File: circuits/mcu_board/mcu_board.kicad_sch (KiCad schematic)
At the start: 80 parts, among them J1 USB_B_Micro, J2 Conn_01x15_Socket, J3 Conn_01x04_Pin, SW1 SW_Push, SW10 SW_Push, SW11 SW_Push, SW12 SW_Push, SW13 SW_Push, SW14 SW_Push, SW3 SW_Push, SW4 SW_Push, SW5 SW_Push, SW6 SW_Push, SW7 SW_Push, SW8 SW_Push, SW9 SW_Push, U1 STM32F302CCTx, U3 74HC165, U4 74HC165, U5 AMS1117-3.3, Y1 8MHz

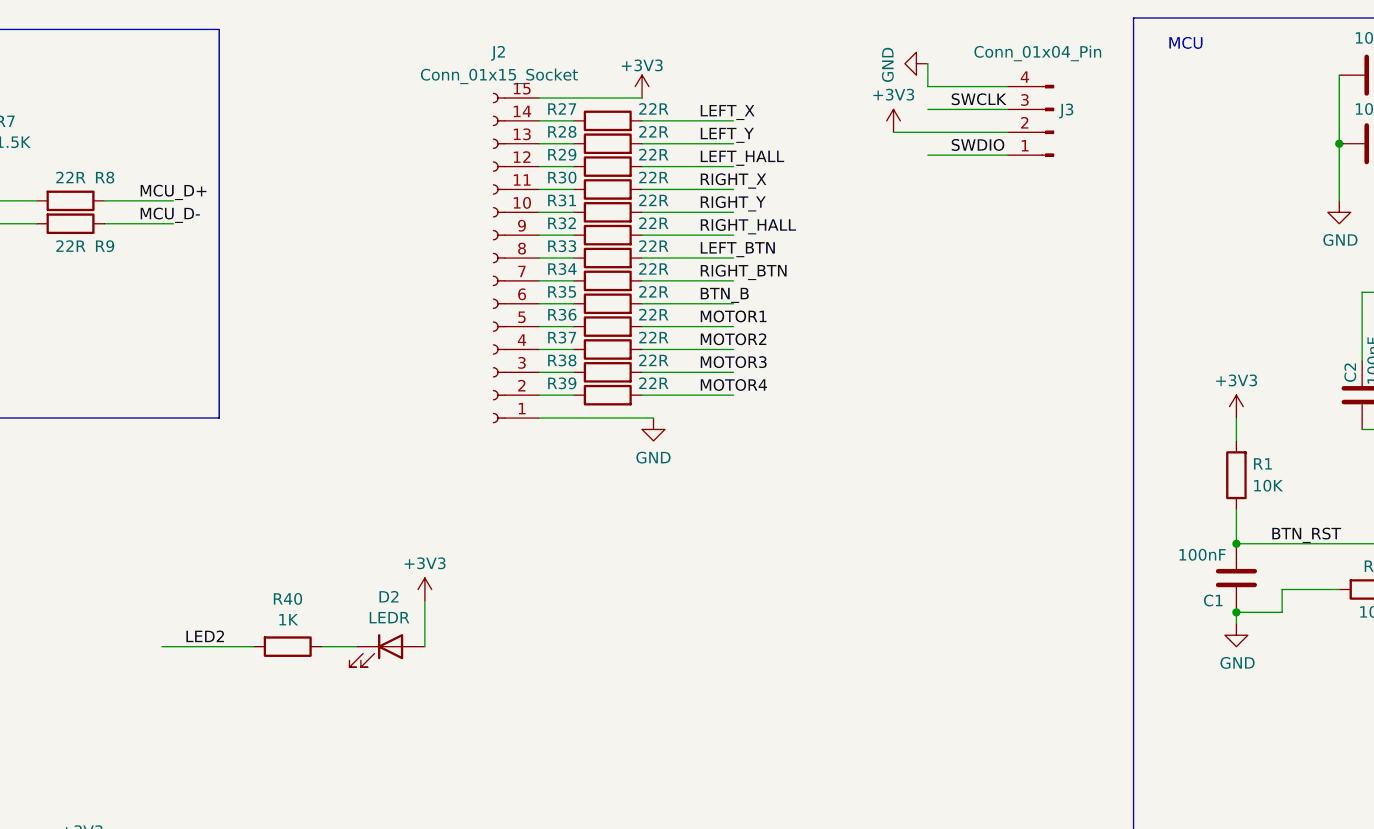
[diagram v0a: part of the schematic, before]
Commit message: pwm和led初步测试ok
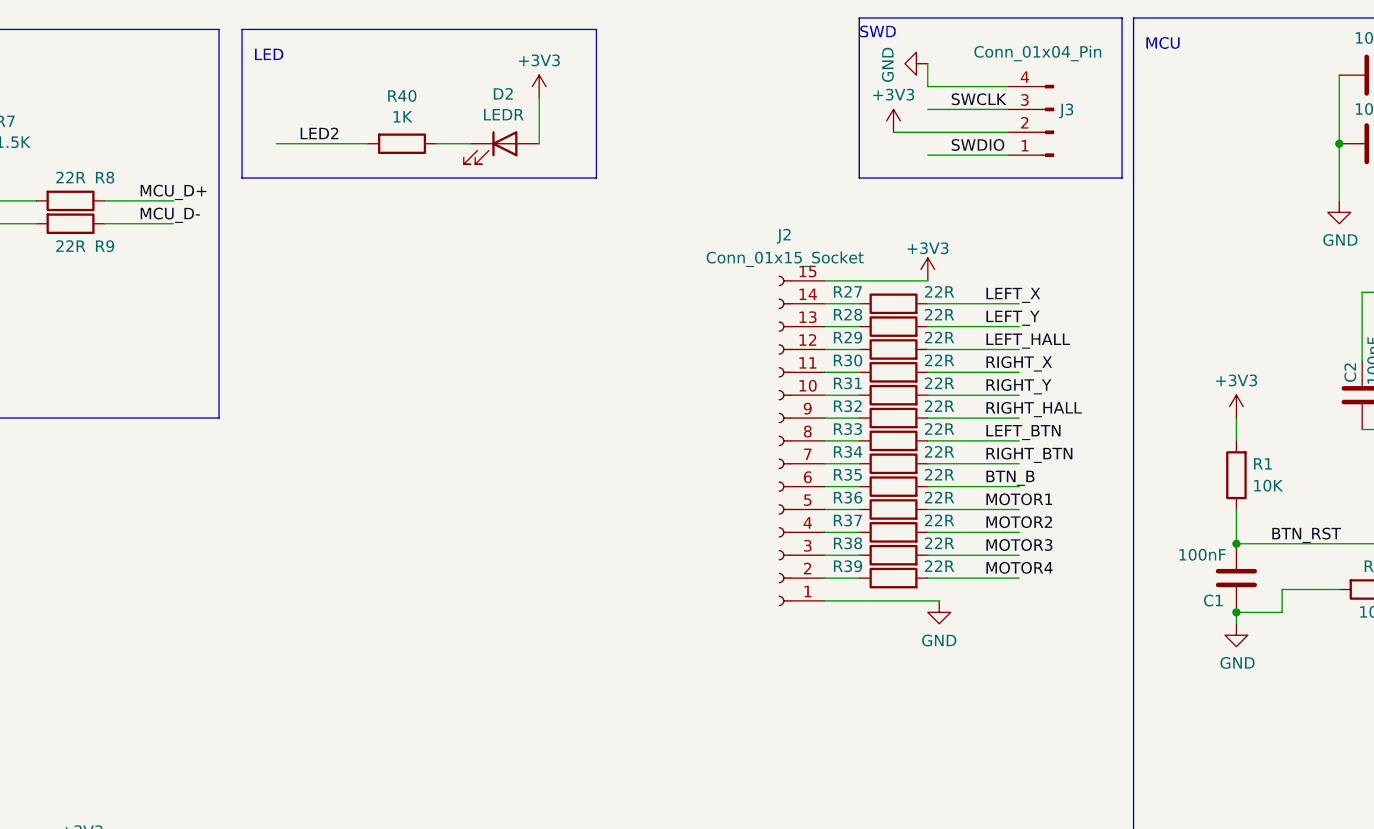
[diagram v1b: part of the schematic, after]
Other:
- note added: "LED"
- note added: "SWD"
- moved on the sheet: D2, J2, R27, R28, R29, R30, R31, R32, R33, R34, R35, R36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

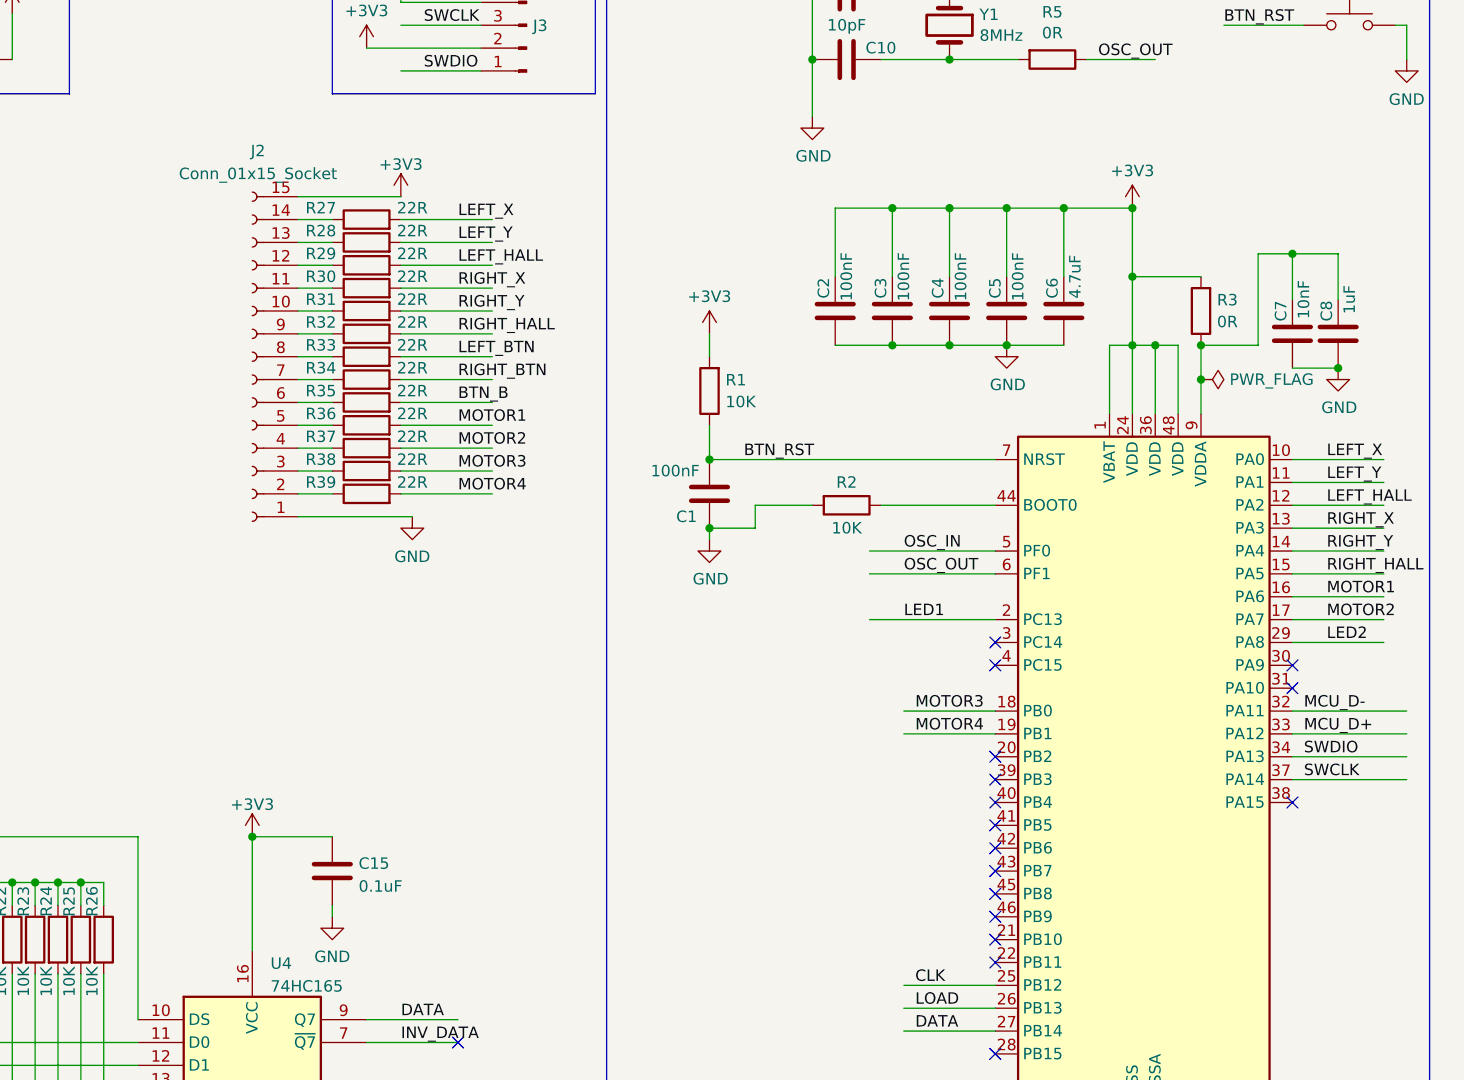
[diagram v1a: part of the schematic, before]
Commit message: layout  摇杆板优化马达驱动,增加覆铜过孔         MCU板改动
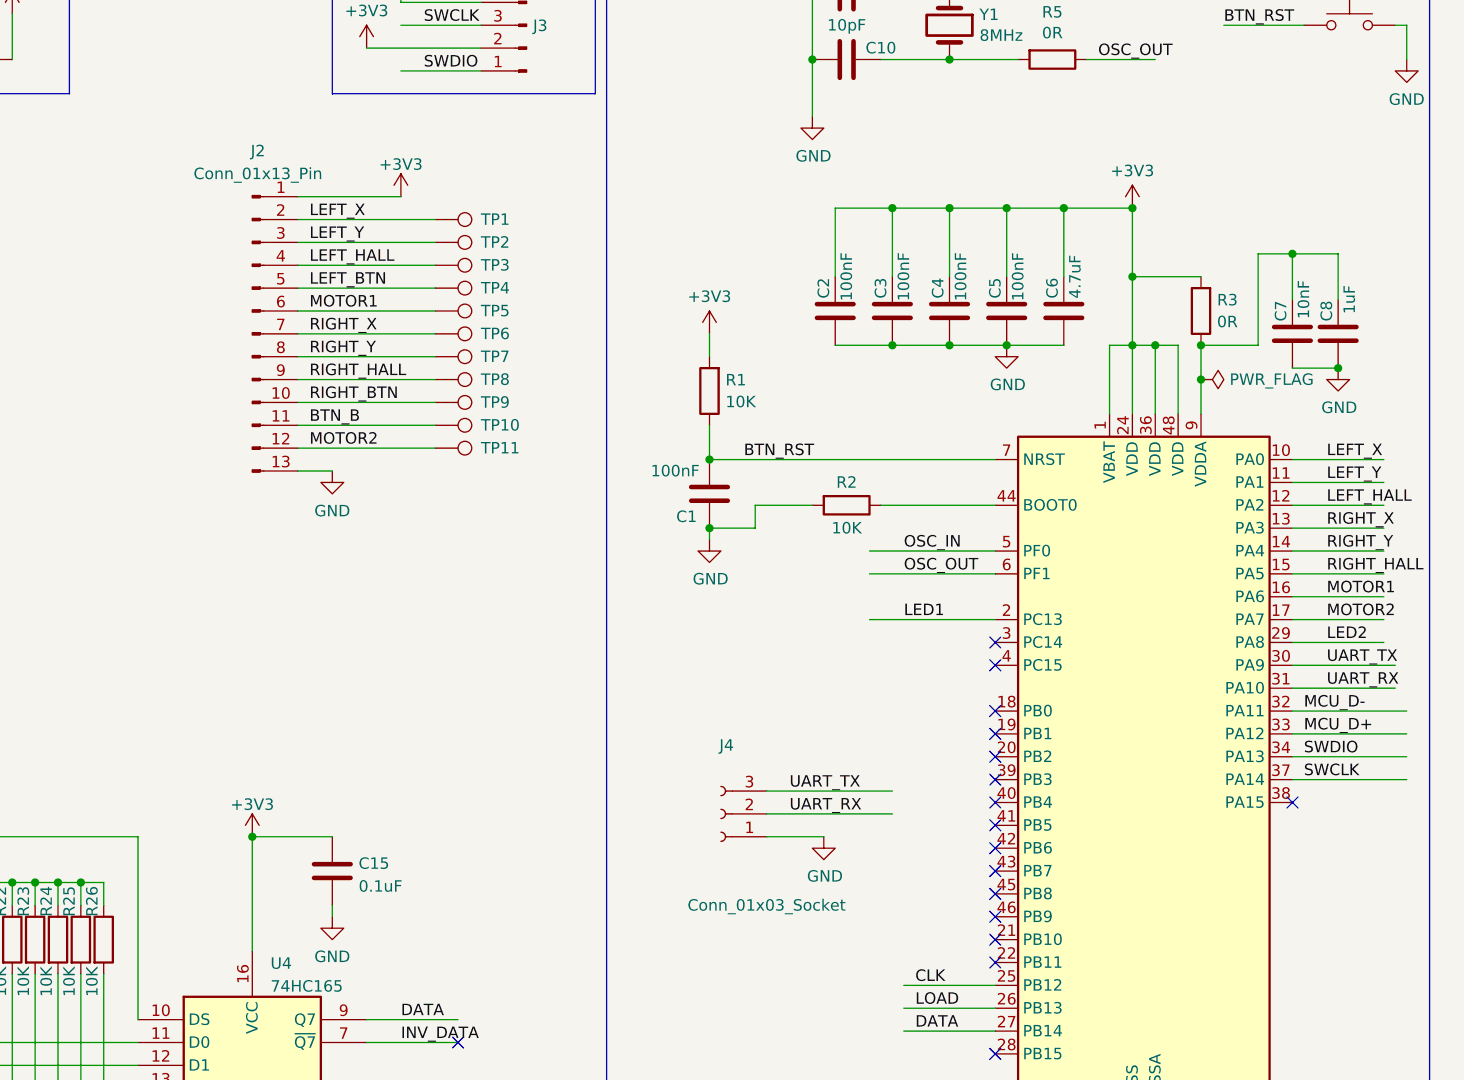
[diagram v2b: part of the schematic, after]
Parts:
- removed J2: Conn_01x15_Socket, symbol Connector:Conn_01x15_Socket
- removed R27, R28, R29, R30, R31, R32, R33, R34, R35, R36, R37, R38, R39: 22R, symbol Device:R
- added J2: Conn_01x13_Pin, Connector_FFC-FPC:Molex_200528-0130_1x13-1MP_P1.00mm_Horizontal, symbol Connector:Conn_01x13_Pin
- added J4: Conn_01x03_Socket, Connector_PinSocket_2.54mm:PinSocket_1x03_P2.54mm_Vertical, symbol Connector:Conn_01x03_Socket
- added TP1, TP10, TP11, TP2, TP3, TP4, TP5, TP6, TP7, TP8, TP9: TestPoint, TestPoint:TestPoint_Pad_1.5x1.5mm, symbol Connector:TestPoint
- C12, C16: footprint (none) -> Capacitor_SMD:C_1206_3216Metric_Pad1.33x1.80mm_HandSolder
- C14, C15: footprint Resistor_SMD:R_0805_2012Metric_Pad1.20x1.40mm_HandSolder -> Capacitor_SMD:C_0805_2012Metric_Pad1.18x1.45mm_HandSolder
- D3: footprint (none) -> Diode_SMD:D_2010_5025Metric_Pad1.52x2.65mm_HandSolder
- SW1, SW10, SW11, SW12, SW13, SW14, SW3, SW4, SW5, SW6, SW7, SW8, SW9: footprint Button_Switch_SMD:SW_Push_1P1T_NO_6x6mm_H9.5mm -> (none)
- SW_Push1: footprint Button_Switch_THT:SW_PUSH_6mm_H4.3mm -> Button_Switch_SMD:SW_Push_1P1T_NO_6x6mm_H9.5mm
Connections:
- net +3V3: now also J2.1 (Pin_1)
- net BTN_B: now also J2.11 (Pin_11), TP10.1
- net GND: now also J2.13 (Pin_13), J4.1 (Pin_1)
- net LEFT_BTN: now also J2.5 (Pin_5), TP4.1
- net LEFT_HALL: now also J2.4 (Pin_4), TP3.1
- net LEFT_X: now also J2.2 (Pin_2), TP1.1
- net LEFT_Y: now also J2.3 (Pin_3), TP2.1
- net MOTOR1: now also J2.6 (Pin_6), TP5.1
- net MOTOR2: now also J2.12 (Pin_12), TP11.1
- net RIGHT_BTN: now also J2.10 (Pin_10), TP9.1
- net RIGHT_HALL: now also J2.9 (Pin_9), TP8.1
- net RIGHT_X: now also J2.7 (Pin_7), TP6.1
- net RIGHT_Y: now also J2.8 (Pin_8), TP7.1
- net UART_TX: now reaches U1.30 (PA9)
- net UART_TX: now also J4.3 (Pin_3)
- net UART_RX: now reaches U1.31 (PA10)
- net UART_RX: now also J4.2 (Pin_2)
- net MOTOR3: no longer names the net of U1.18 (PB0)
- net MOTOR4: no longer names the net of U1.19 (PB1)

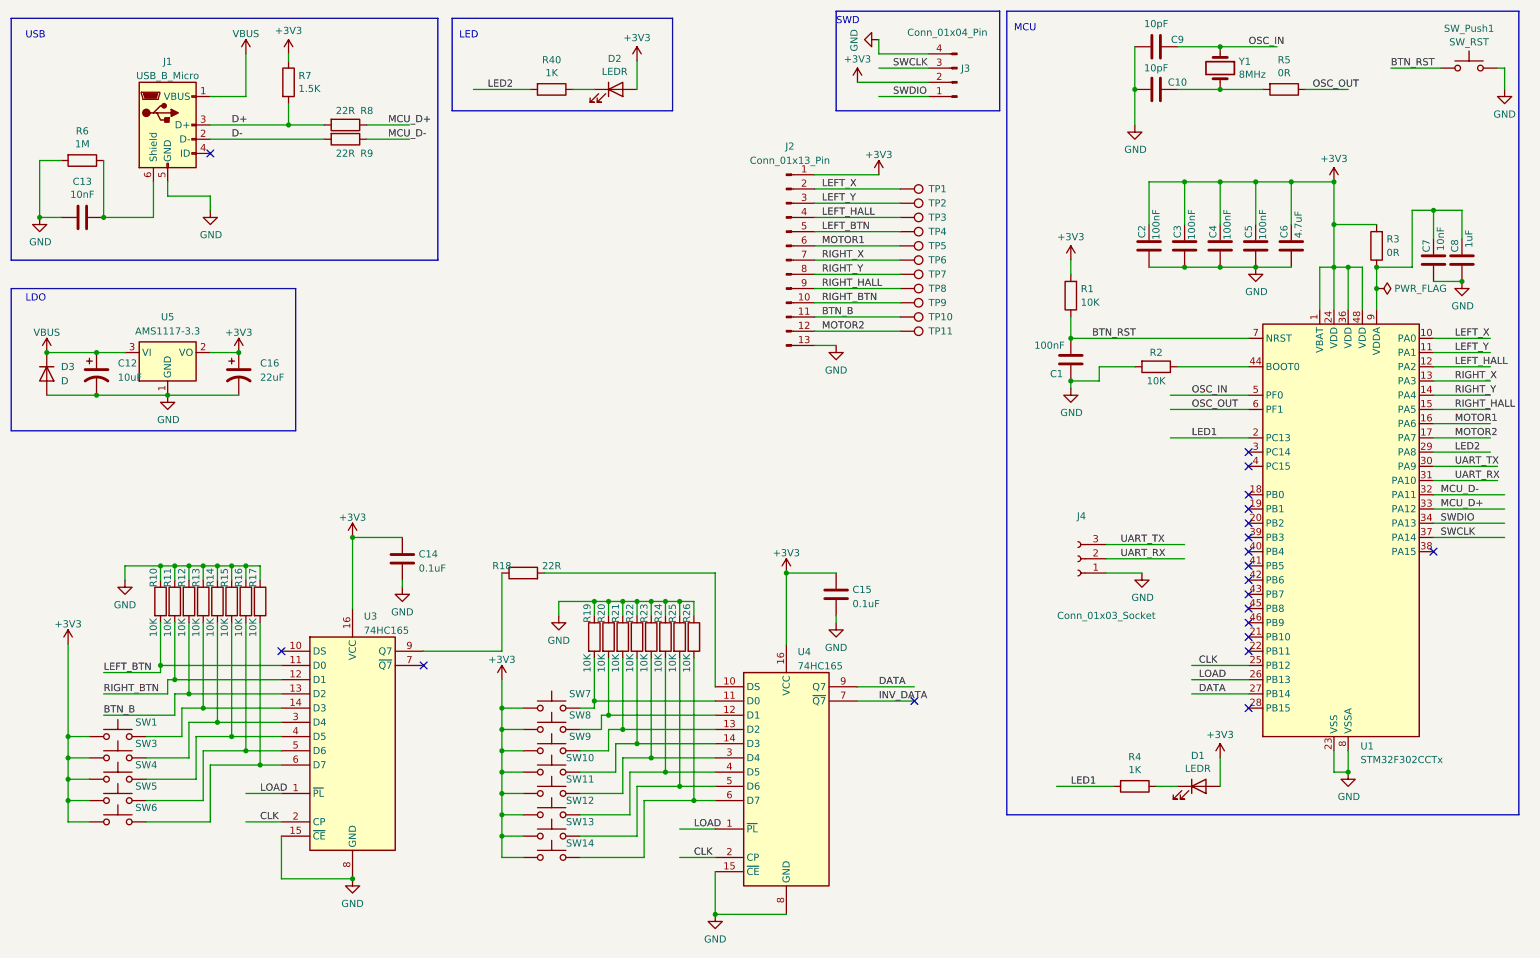
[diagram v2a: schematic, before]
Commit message: mcu板 螺丝孔位置需验证
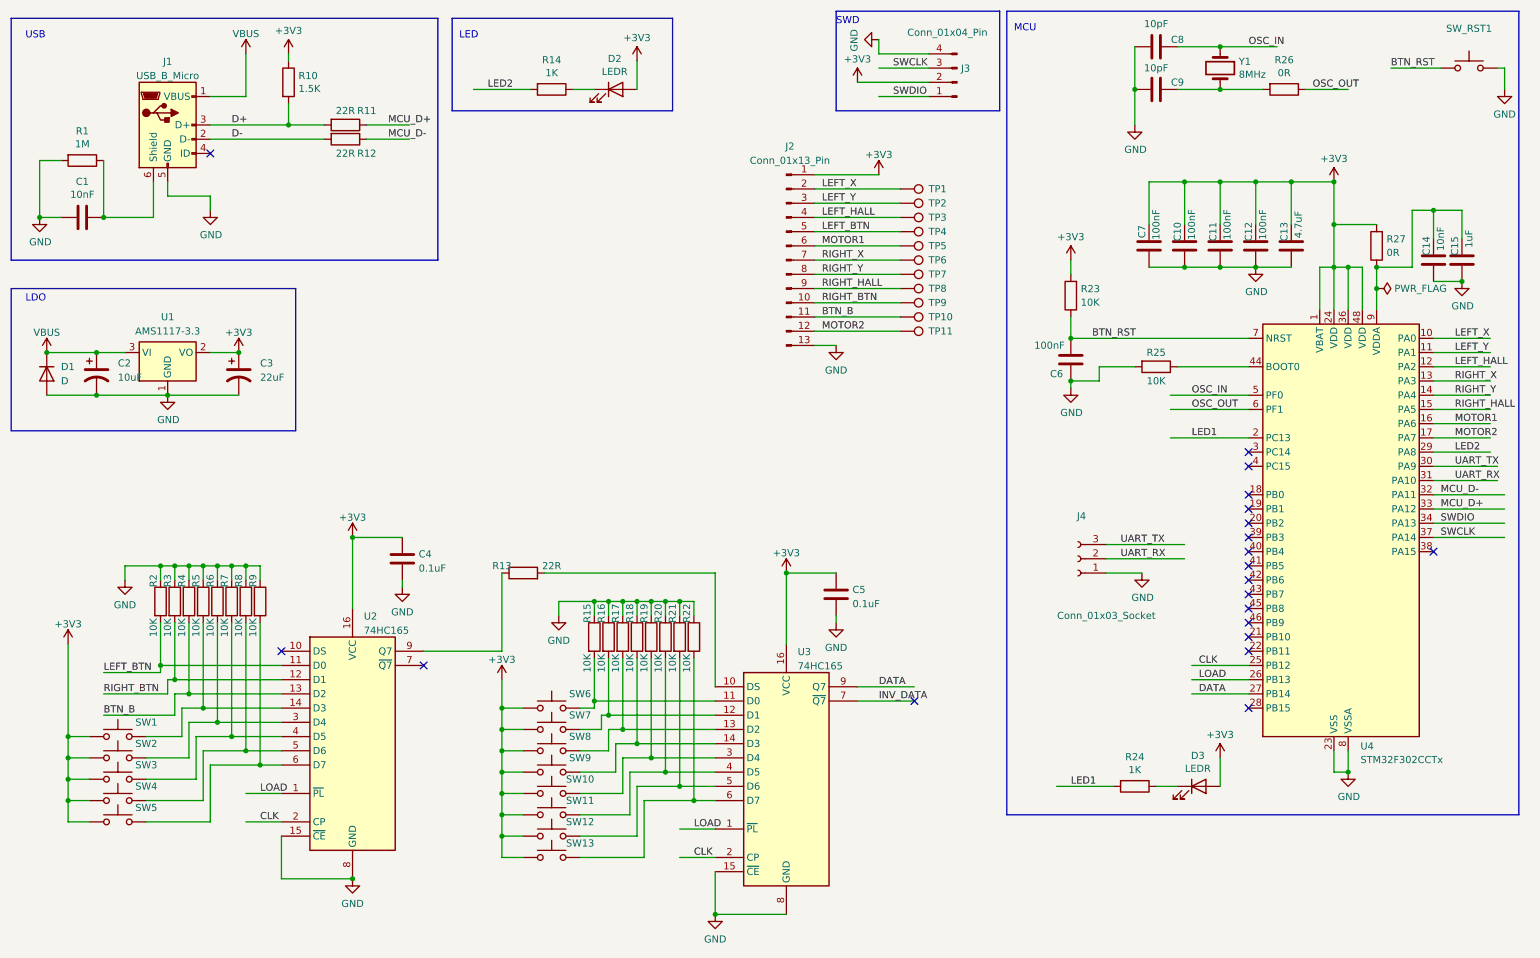
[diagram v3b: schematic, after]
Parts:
- SW1: footprint (none) -> button:touch
- SW10: renamed from SW11; footprint (none) -> button:touch-xbox
- SW11: renamed from SW12; footprint (none) -> Button_Switch_SMD:SW_Push_1P1T_NO_6x6mm_H9.5mm
- SW12: renamed from SW13; footprint (none) -> Button_Switch_SMD:SW_Push_1P1T_NO_6x6mm_H9.5mm
- SW13: renamed from SW14; footprint (none) -> Button_Switch_SMD:SW_Push_1P1T_NO_6x6mm_H9.5mm
- SW2: renamed from SW3; footprint (none) -> button:touch
- SW3: renamed from SW4; footprint (none) -> button:touch
- SW4: renamed from SW5; footprint (none) -> button:touch
- SW5: renamed from SW6; footprint (none) -> button:touch
- SW6: renamed from SW7; footprint (none) -> button:touch-dpad
- SW7: renamed from SW8; footprint (none) -> button:touch-dpad
- SW8: renamed from SW9; footprint (none) -> button:touch-dpad
- SW9: renamed from SW10; footprint (none) -> button:touch-dpad
- renumbered C13 to C1, C3 to C10, C4 to C11, C5 to C12, C6 to C13, C7 to C14, C8 to C15, C12 to C2, C16 to C3, C14 to C4, C15 to C5, C1 to C6, C2 to C7, C9 to C8, C10 to C9, D3 to D1, D1 to D3, R6 to R1, R7 to R10, R8 to R11, R9 to R12, R18 to R13, R40 to R14, R19 to R15, R20 to R16, R21 to R17, R22 to R18, R23 to R19, R10 to R2, R24 to R20, R25 to R21, R26 to R22, R1 to R23, R4 to R24, R2 to R25, R5 to R26, R3 to R27, R11 to R3, R12 to R4, R13 to R5, R14 to R6, R15 to R7, R16 to R8, R17 to R9, SW_Push1 to SW_RST1, U5 to U1, U3 to U2, U4 to U3, U1 to U4

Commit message: layout 增加lb/rb和pair按键封装    空间不够需精简电路
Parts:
- SW11, SW12: footprint Button_Switch_SMD:SW_Push_1P1T_NO_6x6mm_H9.5mm -> button:click_lbrb
- SW13: footprint Button_Switch_SMD:SW_Push_1P1T_NO_6x6mm_H9.5mm -> button:click_pair
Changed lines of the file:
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@@
       (effects (font (size 1.27 1.27)) hide)
     )
-    (property "Footprint" "Button_Switch_SMD:SW_Push_1P1T_NO_6x6mm_H9.5mm" (at 111.76 158.75 0)
+    (property "Footprint" "button:click_pair" (at 111.76 158.75 0)
       (effects (font (size 1.27 1.27)) hide)
     )
@@
       (effects (font (size 1.27 1.27)) hide)
     )
-    (property "Footprint" "Button_Switch_SMD:SW_Push_1P1T_NO_6x6mm_H9.5mm" (at 111.76 154.94 0)
+    (property "Footprint" "button:click_lbrb" (at 111.76 154.94 0)
       (effects (font (size 1.27 1.27)) hide)
     )
@@
       (effects (font (size 1.27 1.27)) hide)
     )
-    (property "Footprint" "Button_Switch_SMD:SW_Push_1P1T_NO_6x6mm_H9.5mm" (at 111.76 151.13 0)
-      (effects (font (size 1.27 1.27)) hide)
-    )
+    (property "Footprint" "button:click_lbrb" (at 111.76 151.13 0)
+      (effects (font (size 1.27 1.27)) hide)
+    )
